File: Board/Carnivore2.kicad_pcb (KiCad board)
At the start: 2 copper layers, 157 parts, among them T1 2SC945, T2 2SA733, T3 2SC945, T4 2SC945, T5 2SC945, T6 2SA733, U7 50 MHz

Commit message: Schematic and pcb conversion cleanup and rework
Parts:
- removed ?: , 
- removed LED2, LED3, LED4: , C_0603_1
- AU1, AU2, LED1, U1, U2, U3, U4, U5, U6, XC1: value (none) -> ~
- B1: renamed from ?; value (none) -> BAT
- H1, H2: renamed from ?; value (none) -> MountingHole
- J1: renamed from .3; value (none) -> Conn_01x02_Pin
- TP1, TP2: renamed from ?; value (none) -> TestPoint
- U8: renamed from .1; value (none) -> DNI; footprint KNS01_1 -> Oscillator:Oscillator_SMD_TXC_7C-4Pin_5.0x3.2mm_HandSoldering
- X1: renamed from .2; value (none) -> EDGE50/MSX
- X2: renamed from .6; value (none) -> HEADER_5X2; footprint IDC10M_1 -> HDR2X5
- X3: renamed from .7; value (none) -> HEADER_5X2; footprint IDC10M_1 -> HDR2X5
- moved U8 3.69 mm to (144.3, 76.5), turned to 180 degrees
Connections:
- net +AV12 renamed /AV12+
- net -AV12 renamed /AV12-
- net -V12 renamed /VCC-12
- net A0 renamed Net-(R9-Pad2)
- net A1 renamed Net-(R36-Pad2)
- net A10 renamed Net-(R13-Pad2)
- net A11 renamed Net-(R32-Pad2)
- net A12 renamed Net-(R34-Pad2)
- net A13 renamed Net-(R10-Pad2)
- net A14 renamed Net-(R35-Pad2)
- net A15 renamed Net-(R14-Pad2)
- net A2 renamed Net-(R8-Pad2)
- net A3 renamed Net-(R37-Pad2)
- net A4 renamed Net-(R7-Pad2)
- net A5 renamed Net-(R38-Pad2)
- net A6 renamed Net-(R12-Pad2)
- net A7 renamed Net-(R33-Pad2)
- net A8 renamed Net-(R11-Pad2)
- net A9 renamed Net-(R31-Pad2)
- net ADSO renamed /ASDO
- net BICK renamed /BICK
- net CE2 renamed Net-(D4-K)
- net CF_LED renamed Net-(LED1-K)
- net CKS renamed /CKS
- net CLC renamed Net-(R2-Pad2)
- net CONF_DONE renamed /CONF_DONE
- net D0 renamed Net-(R6-Pad2)
- net D1 renamed Net-(R39-Pad2)
- net D2 renamed Net-(R5-Pad2)
- net D3 renamed Net-(R40-Pad2)
- net D4 renamed Net-(R4-Pad2)
- net D5 renamed Net-(R41-Pad2)
- net D6 renamed Net-(R3-Pad2)
- net D7 renamed Net-(R42-Pad2)
- net DATA0 renamed /DATA0
- net DCLK renamed /DCLK
- net EECK renamed /EECK
- net EECS renamed /EECS
- net EEDI renamed /EEDI
- net EEDO renamed /EEDO
- net HD10 renamed /HD10
- net HD11 renamed /HD11
- net HD12 renamed /HD12
- net HD13 renamed /HD13
- net HD14 renamed /HD14
- net HD15 renamed /HD15
- net HD3 renamed /HD03
- net HD4 renamed /HD04
- net HD5 renamed /HD05
- net HD6 renamed /HD06
- net HD7 renamed /HD07
- net KN0 renamed /KN0
- net LAUDIOR renamed Net-(T5-E)
- net LAUDOL renamed Net-(T3-E)
- net LRCK renamed /LRCK
- net MCLK renamed /MCLK
- net NCE renamed /NCE
- net NCONFIG renamed /NCONFIG
- net NCS0 renamed /NCSO
- net NET00000 renamed /CLC50
- net NET00004 renamed Net-(T1-B)
- net NET00005 renamed Net-(T1-C)
- net NET00006 renamed Net-(T2-B)
- net NET00007 renamed Net-(X1-Pad44)
- net NET00008 renamed Net-(T2-C)
- net NET00018 renamed Net-(U1D-VCCA_PLL1)
- net NET00019 renamed Net-(U1D-VCCA_PLL2)
- net NET00020 renamed /~{HREG}
- net NET00024 renamed Net-(D3-K)
- net NET00025 renamed Net-(C23-PLUS)
- net NET00026 renamed Net-(LED1-A)
- net NET00027 renamed Net-(AU1A-IN+)
- net NET00028 renamed Net-(AU1A-IN-)
- net NET00029 renamed Net-(C102-Pad1)
- net NET00031 renamed Net-(C103-PLUS)
- net NET00033 renamed Net-(AU2A-IN-)
- net NET00036 renamed Net-(AU1B-IN+)
- net NET00037 renamed Net-(AU1B-IN-)
- net NET00038 renamed Net-(C202-Pad1)
- net NET00040 renamed Net-(C203-PLUS)
- net NET00041 renamed Net-(AU2B-IN-)
- net NET00042 renamed Net-(C205-MINUS)
- net NET00045 renamed Net-(AU2B-OUT)
- net NET00046 renamed Net-(C105-MINUS)
- net NET00047 renamed Net-(T5-B)
- net NET00048 renamed Net-(T4-B)
- net NET00049 renamed Net-(T3-B)
- net NET00050 renamed Net-(T6-C)
- net NET00051 renamed Net-(C29-PLUS)
- net NET00054 renamed Net-(U5-AOUTR)
- net NET00055 renamed Net-(U5-AOUTL)
- net NET00057 renamed Net-(C26-PLUS)
- net NET00058 renamed Net-(AU2A-OUT)
- net NSTATUS renamed Net-(U1C-nSTATUS)
- net RA0 renamed /RA00
- net RA1 renamed /RA01
- net RA10 renamed /RA10
- net RA11 renamed /RA11
- net RA12 renamed /RA12
- net RA13 renamed /RA13
- net RA14 renamed /RA14
- net RA15 renamed /RA15
- net RA16 renamed /RA16
- net RA17 renamed /RA17
- net RA18 renamed /RA18
- net RA19 renamed /RA19
- net RA2 renamed /RA02
- net RA20 renamed /RA20
- net RA21 renamed /RA21
- net RA3 renamed /RA03
- net RA4 renamed /RA04
- net RA5 renamed /RA05
- net RA6 renamed /RA06
- net RA7 renamed /RA07
- net RA8 renamed /RA08
- net RA9 renamed /RA09
- net RDQ0 renamed /RDQ0
- net RDQ1 renamed /RDQ1
- net RDQ15A-1 renamed /RDQ15A-1
- net RDQ2 renamed /RDQ2
- net RDQ3 renamed /RDQ3
- net RDQ4 renamed /RDQ4
- net RDQ5 renamed /RDQ5
- net RDQ6 renamed /RDQ6
- net RDQ7 renamed /RDQ7
- net RSW1 renamed Net-(R15-Pad2)
- net RSW2 renamed Net-(R25-Pad2)
- net RVPPE renamed /RVPPE
- net R~E renamed /R~{E}
- net R~G renamed /R~{G}
- net R~RB renamed /~{RRB}
- net R~RP renamed /~{RRP}
- net R~W renamed /~{RWR}
- net SDATA renamed /SDATA
- net SLTA0 renamed /SLT_A00
- net SLTA1 renamed /SLT_A01
- net SLTA10 renamed /SLT_A10
- net SLTA11 renamed /SLT_A11
- net SLTA12 renamed /SLT_A12
- net SLTA13 renamed /SLT_A13
- net SLTA14 renamed /SLT_A14
- net SLTA15 renamed /SLT_A15
- net SLTA2 renamed /SLT_A02
- net SLTA3 renamed /SLT_A03
- net SLTA4 renamed /SLT_A04
- net SLTA5 renamed /SLT_A05
- net SLTA6 renamed /SLT_A06
- net SLTA7 renamed /SLT_A07
- net SLTA8 renamed /SLT_A08
- net SLTA9 renamed /SLT_A09
- net SLTCLC renamed /SLT_CLC
- net SLTD0 renamed /SLT_D0
- net SLTD1 renamed /SLT_D1
- net SLTD2 renamed /SLT_D2
- net SLTD3 renamed /SLT_D3
- net SLTD4 renamed /SLT_D4
- net SLTD5 renamed /SLT_D5
- net SLTD6 renamed /SLT_D6
- net SLTD7 renamed /SLT_D7
- net SLTRSW2 renamed /RSW2
- net SLTSOUND renamed /SLTSOUND
- net SLT_MREQ renamed /~{SLT_MREQ}
- net SLT~BUSDIR renamed /~{SLT_BUSDIR}
- net SLT~CS1 renamed /~{SLT_CS1}
- net SLT~CS12 renamed /~{SLT_CS12}
- net SLT~CS2 renamed /~{SLT_CS2}
- net SLT~INT renamed /~{SLT_INT}
- net SLT~IORQ renamed /~{SLT_IORQ}
- net SLT~M1 renamed /~{SLT_M1}
- net SLT~RD renamed /~{SLT_RD}
- net SLT~RFSH renamed /~{SLT_RFSH}
- net SLT~SLTSL renamed /~{SLT_SLTSEL}
- net SLT~WAIT renamed /~{SLT_WAIT}
- net SLT~WR renamed /~{SLT_WR}
- net STLRSW1 renamed /RSW1
- net TCK renamed /TCK
- net TDI renamed /TDI
- net TDO renamed /TDO
- net TMS renamed /TMS
- net V1.2 renamed /VCC1.2
- net V12 renamed /VCC+12
- net VCCRAM renamed Net-(D1-K)
- net VDDDA renamed /VCC3.3A
- net VPP12 renamed Net-(U2-Vpp/~{WP})
- net ~BUSDIR renamed Net-(R18-Pad2)
- net ~CS1 renamed Net-(R23-Pad2)
- net ~CS12 renamed Net-(R24-Pad2)
- net ~CS2 renamed Net-(R22-Pad2)
- net ~CSRAM renamed /~{CSRAM}
- net ~HCS1 renamed /~{HCS1}
- net ~HCS3 renamed /~{HCS3}
- net ~HRD renamed /~{HRD}
- net ~HRST renamed /~{HRST}
- net ~IC renamed /~{IC}
- net ~INT renamed Net-(R19-Pad2)
- net ~IORQ renamed Net-(R28-Pad2)
- net ~M1 renamed Net-(R27-Pad2)
- net ~MREQ renamed Net-(R17-Pad2)
- net ~RD renamed Net-(R16-Pad2)
- net ~RFSH renamed Net-(R20-Pad2)
- net ~SLTSL renamed Net-(R21-Pad2)
- net ~WAIT renamed Net-(R26-Pad2)
- net ~WR renamed Net-(R29-Pad2)
- AU2 pad 3: GND -> /GND
- AU2 pad 5: GND -> /GND
- AX1 pad 1: GND -> /GND
- C1 pad 1: GND -> /GND
- C1 pad 2: VCC5 -> /VCC5
- C10 pad 1: V3.3 -> /VCC3.3
- C10 pad 2: GND -> /GND
- C101 pad 1: GND -> /GND
- C102 pad 2: GND -> /GND
- C11 pad 2: GND -> /GND
- C12 pad 1: GND -> /GND
- C13 pad 1: GND -> /GND
- C14 pad 2: GND -> /GND
- C15 pad 2: GND -> /GND
- C16 pad 1: GND -> /GND
- C16 pad 2: V3.3 -> /VCC3.3
- C17 pad 2: GND -> /GND
- C18 pad 1: GND -> /GND
- C19 pad 2: GND -> /GND
- C2 pad 1: GND -> /GND
- C2 pad 2: V3.3 -> /VCC3.3
- C20 pad 1: GND -> /GND
- C201 pad 1: GND -> /GND
- C202 pad 2: GND -> /GND
- C21 pad 2: GND -> /GND
- C22 pad 1: GND -> /GND
- C23 pad 1: GND -> /GND
- C24 pad 1: GND -> /GND
- C25 pad 1: GND -> /GND
- C26 pad 1: GND -> /GND
- C27 pad 1: GND -> /GND
- C28 pad 1: GND -> /GND
- C28 pad 2: NET00053 -> Net-(C28-PLUS)
- C29 pad 1: GND -> /GND
- C3 pad 1: GND -> /GND
- C30 pad 1: GND -> /GND
- C30 pad 2: V3.3 -> /VCC3.3
- C4 pad 1: GND -> /GND
- C4 pad 2: V3.3 -> /VCC
- C5 pad 1: GND -> /GND
- C5 pad 2: V3.3 -> /VCC
- C6 pad 1: GND -> /GND
- C7 pad 1: GND -> /GND
- C7 pad 2: V3.3 -> /VCC3.3
- C8 pad 1: GND -> /GND
- C8 pad 2: V3.3 -> /VCC3.3
- C9 pad 1: GND -> /GND
- C9 pad 2: V3.3 -> /VCC3.3
- D1 pad 1: V3.3 -> /VCC3.3
- D2 pad 1: NET00022 -> Net-(D2-A)
- D3 pad 1: V3.3 -> /VCC3.3
- D5 pad 1: NET00053 -> Net-(D5-A)
- D5 pad 2: ~RESET -> /~{SLT_RESET}
- D6 pad 1: VCC5 -> /VCC5
- R30 pad 1: SLT~RESET -> /~{SLT_RESET}
- R30 pad 2: ~RESET -> Net-(R30-Pad2)
- R45 pad 2: V3.3 -> /VCC3.3
- R46 pad 1: GND -> /GND
- R47 pad 1: V3.3 -> /VCC3.3
- R48 pad 1: V3.3 -> /VCC3.3
- R50 pad 1: GND -> /GND
- R51 pad 1: NET00023 -> Net-(B1-PadPOS)
- R51 pad 2: NET00022 -> Net-(D2-A)
- R57 pad 1: GND -> /GND
- R58 pad 1: V3.3 -> /VCC3.3
- R59 pad 1: V3.3 -> /VCC3.3
- R60 pad 1: NET00052 -> Net-(C28-PLUS)
- R60 pad 2: NET00053 -> Net-(D5-A)
- R65 pad 1: VCC5 -> /VCC5
- R65 pad 2: NET00052 -> Net-(C28-PLUS)
- R66 pad 2: V3.3 -> /VCC3.3
- T1 pad A2: GND -> /GND
- T3 pad K: GND -> /GND
- T4 pad K: GND -> /GND
- T5 pad K: GND -> /GND
- T6 pad A1: NET00052 -> Net-(C28-PLUS)
- U1 pad 10: (no net) -> unconnected-(U1A-IO,_LVDS7n,_DQ1L1/_-Pad10)
- U1 pad 100: GND -> /GND
- U1 pad 107: (no net) -> unconnected-(U1B-IO,_LVDS41n_(INIT_DONE)-Pad107)
- U1 pad 109: V3.3 -> /VCC3.3
- U1 pad 11: (no net) -> unconnected-(U1A-IO,_LVDS6p,_DQ1L2/_-Pad11)
- U1 pad 111: GND -> /GND
- U1 pad 122: V3.3 -> /VCC3.3
- U1 pad 124: GND -> /GND
- U1 pad 125: GND -> /GND
- U1 pad 126: GND -> /GND
- U1 pad 129: (no net) -> /GND
- U1 pad 131: (no net) -> /GND
- U1 pad 132: (no net) -> /GND
- U1 pad 136: V3.3 -> /VCC3.3
- U1 pad 140: GND -> /GND
- U1 pad 148: V3.3 -> /VCC3.3
- U1 pad 153: GND -> /GND
- U1 pad 154: GND -> /GND
- U1 pad 156: GND -> /GND
- U1 pad 158: GND -> /GND
- U1 pad 159: GND -> /GND
- U1 pad 166: V3.3 -> /VCC3.3
- U1 pad 167: GND -> /GND
- U1 pad 170: HD9 -> /HD09
- U1 pad 171: HD2 -> /HD02
- U1 pad 172: V3.3 -> /VCC3.3
- U1 pad 173: HD8 -> /HD08
- U1 pad 174: GND -> /GND
- U1 pad 175: HD1 -> /HD01
- U1 pad 176: HD0 -> /HD00
- U1 pad 177: GND -> /GND
- U1 pad 179: HA0 -> /~{HA0}
- U1 pad 181: HA1 -> /~{HA1}
- U1 pad 182: HA2 -> /~{HA2}
- U1 pad 183: V3.3 -> /VCC3.3
- U1 pad 184: GND -> /GND
- U1 pad 186: GND -> /GND
- U1 pad 188: ~HWR -> /~{HVR}
- U1 pad 189: (no net) -> unconnected-(U1A-IO,_LVDS19n,_DQ1T2/DQ1T11-Pad189)
- U1 pad 194: V3.3 -> /VCC3.3
- U1 pad 196: GND -> /GND
- U1 pad 202: V3.3 -> /VCC3.3
- U1 pad 204: GND -> /GND
- U1 pad 23: (no net) -> /GND
- U1 pad 24: (no net) -> /GND
- U1 pad 25: GND -> /GND
- U1 pad 28: (no net) -> /GND
- U1 pad 29: V3.3 -> /VCC3.3
- U1 pad 3: (no net) -> unconnected-(U1A-IO,_LVDS9p_(CRC_ERROR)-Pad3)
- U1 pad 36: (no net) -> unconnected-(U1A-IO,_LVDS2n-Pad36)
- U1 pad 37: (no net) -> unconnected-(U1A-IO,_VREFB1N1-Pad37)
- U1 pad 38: GND -> /GND
- U1 pad 4: (no net) -> unconnected-(U1A-IO,_LVDS9n_(CLKUSR)-Pad4)
- U1 pad 40: (no net) -> unconnected-(U1A-IO,_LVDS1p,_DQ1L8/_-Pad40)
- U1 pad 41: (no net) -> unconnected-(U1A-IO,_LVDS1n,_(DM1L/BWS#1L)/_-Pad41)
- U1 pad 42: V3.3 -> /VCC3.3
- U1 pad 43: (no net) -> unconnected-(U1A-IO-Pad43)
- U1 pad 44: (no net) -> unconnected-(U1A-IO,_LVDS0p-Pad44)
- U1 pad 46: (no net) -> unconnected-(U1A-IO-Pad46)
- U1 pad 47: (no net) -> unconnected-(U1A-IO,_PLL1_OUTp-Pad47)
- U1 pad 48: (no net) -> unconnected-(U1A-IO,_PLL1_OUTn-Pad48)
- U1 pad 49: GND -> /GND
- U1 pad 5: (no net) -> unconnected-(U1A-IO,_LVDS8p-Pad5)
- U1 pad 50: GND -> /GND
- U1 pad 52: GND -> /GND
- U1 pad 54: GND -> /GND
- U1 pad 55: GND -> /GND
- U1 pad 6: (no net) -> unconnected-(U1A-IO,_LVDS8n-Pad6)
- U1 pad 62: V3.3 -> /VCC3.3
- U1 pad 65: GND -> /GND
- U1 pad 7: V3.3 -> /VCC3.3
- U1 pad 71: V3.3 -> /VCC3.3
- U1 pad 73: GND -> /GND
- U1 pad 78: GND -> /GND
- U1 pad 8: (no net) -> unconnected-(U1A-IO,_LVDS7p,_DQ1L0/_-Pad8)
- U1 pad 83: V3.3 -> /VCC3.3
- U1 pad 85: GND -> /GND
- U1 pad 89: SLT~RESET -> /~{SLT_RESET}
- U1 pad 9: GND -> /GND
- U1 pad 91: V3.3 -> /VCC3.3
- U1 pad 93: GND -> /GND
- U1 pad 98: V3.3 -> /VCC3.3
- U2 pad 27: GND -> /GND
- U2 pad 30: RDQ8 -> unconnected-(U2-D8-Pad30)
- U2 pad 32: RDQ9 -> unconnected-(U2-D9-Pad32)
- U2 pad 34: RDQ10 -> unconnected-(U2-D10-Pad34)
- U2 pad 36: RDQ11 -> unconnected-(U2-D11-Pad36)
- U2 pad 37: V3.3 -> /VCC3.3
- U2 pad 39: RDQ12 -> unconnected-(U2-D12-Pad39)
- U2 pad 41: RDQ13 -> unconnected-(U2-D13-Pad41)
- U2 pad 43: RDQ14 -> unconnected-(U2-D14-Pad43)
- U2 pad 46: GND -> /GND
- U2 pad 47: GND -> /GND
- U3 pad 10: (no net) -> unconnected-(U3-NC-Pad10)
- U3 pad 13: (no net) -> unconnected-(U3-DNU-Pad13)
- U3 pad 14: (no net) -> unconnected-(U3-~{BNE}-Pad14)
- U3 pad 15: (no net) -> unconnected-(U3-~{BLE}-Pad15)
- U3 pad 27: GND -> /GND
- U3 pad 30: (no net) -> unconnected-(U3-D8-Pad30)
- U3 pad 32: (no net) -> unconnected-(U3-D9-Pad32)
- U3 pad 34: (no net) -> unconnected-(U3-D10-Pad34)
- U3 pad 36: (no net) -> unconnected-(U3-D11-Pad36)
- U3 pad 39: (no net) -> unconnected-(U3-D12-Pad39)
- U3 pad 41: (no net) -> unconnected-(U3-D13-Pad41)
- U3 pad 43: (no net) -> unconnected-(U3-D14-Pad43)
- U3 pad 46: GND -> /GND
- U3 pad 47: GND -> /GND
- U4 pad 3: V3.3 -> /VCC3.3
- U4 pad 4: GND -> /GND
- U4 pad 7: V3.3 -> /VCC3.3
- U4 pad 8: V3.3 -> /VCC3.3
- U5 pad 1: GND -> /GND
- U5 pad 11: (no net) -> unconnected-(U5-nc-Pad11)
- U5 pad 12: (no net) -> unconnected-(U5-nc-Pad12)
- U5 pad 13: (no net) -> unconnected-(U5-nc-Pad13)
- U5 pad 14: (no net) -> unconnected-(U5-nc-Pad14)
- U5 pad 19: GND -> /GND
- U5 pad 20: (no net) -> unconnected-(U5-nc-Pad20)
- U5 pad 21: (no net) -> unconnected-(U5-nc-Pad21)
- U5 pad 23: GND -> /GND
- U5 pad 24: (no net) -> unconnected-(U5-TST2-Pad24)
- U5 pad 3: GND -> /GND
- U6 pad 5: GND -> /GND
- U6 pad 6: GND -> /GND
- U6 pad 7: (no net) -> unconnected-(U6-DU-Pad7)
- U6 pad 8: V3.3 -> /VCC3.3
- U7 pad 1: (no net) -> unconnected-(U7-~{ST}-Pad1)
- U7 pad 2: GND -> /GND
- U7 pad 4: V3.3 -> /VCC3.3
- U8 pad 1: (no net) -> unconnected-(U8-~{ST}-Pad1)
- U8 pad 2: (no net) -> /GND
- U8 pad 4: GND -> /VCC3.3
- UCT1 pad 1: GND -> /GND
- UCT1 pad 3: VCC5 -> /VCC5
- UCT2 pad 1: GND -> /GND
- UCT2 pad 2: V3.3 -> /VCC3.3
- UCT2 pad 3: VCC5 -> /VCC5
- UCT2 pad 4: V3.3 -> /VCC3.3
- UCT3 pad 1: GND -> /GND
- UCT3 pad 3: VCC5 -> /VCC5
- X1 pad 15: ~RESET -> Net-(R30-Pad2)
- X1 pad 41: GND -> /GND
- X1 pad 43: GND -> /GND
- X1 pad 45: VCC5 -> /VCC5
- X1 pad 47: VCC5 -> /VCC5
- X2 pad 10: GND -> /GND
- X2 pad 2: GND -> /GND
- X2 pad 4: V3.3 -> /VCC3.3
- X3 pad 10: GND -> /GND
- X3 pad 2: GND -> /GND
- X3 pad 4: V3.3 -> /VCC3.3
- X3 pad 6: (no net) -> unconnected-(X3-Pad6)
- X3 pad 7: (no net) -> unconnected-(X3-Pad7)
- X3 pad 8: (no net) -> unconnected-(X3-Pad8)
- XC1 pad 1: GND -> /GND
- XC1 pad 10: GND -> /GND
- XC1 pad 11: GND -> /GND
- XC1 pad 12: GND -> /GND
- XC1 pad 13: V3.3 -> /VCC
- XC1 pad 14: GND -> unconnected-(XC1-Pad14)
- XC1 pad 15: GND -> /GND
- XC1 pad 16: GND -> /GND
- XC1 pad 17: GND -> /GND
- XC1 pad 18: HA2 -> /HA2
- XC1 pad 19: HA1 -> /HA1
- XC1 pad 20: HA0 -> /HA0
- XC1 pad 21: HD0 -> /HD0
- XC1 pad 22: HD1 -> /HD1
- XC1 pad 23: HD2 -> /HD2
- XC1 pad 24: (no net) -> unconnected-(XC1-Pad24)
- XC1 pad 25: (no net) -> unconnected-(XC1-Pad25)
- XC1 pad 26: (no net) -> unconnected-(XC1-Pad26)
- XC1 pad 33: GND -> /GND
- XC1 pad 35: ~HWR -> /~{HWR}
- XC1 pad 36: (no net) -> unconnected-(XC1-Pad36)
- XC1 pad 37: (no net) -> unconnected-(XC1-Pad37)
- XC1 pad 38: V3.3 -> /VCC
- XC1 pad 39: GND -> /GND
- XC1 pad 40: (no net) -> unconnected-(XC1-Pad40)
- XC1 pad 42: (no net) -> unconnected-(XC1-Pad42)
- XC1 pad 43: (no net) -> unconnected-(XC1-Pad43)
- XC1 pad 46: (no net) -> unconnected-(XC1-Pad46)
- XC1 pad 47: HD8 -> /HD8
- XC1 pad 48: HD9 -> /HD9
- XC1 pad 50: GND -> /GND
- XC1 pad 51: GND -> unconnected-(XC1-MH1-Pad51)
- XC1 pad 52: GND -> unconnected-(XC1-MH2-Pad52)
- XC1 pad 53: (no net) -> unconnected-(XC1-MH3-Pad53)
- XC1 pad 54: (no net) -> unconnected-(XC1-MH4-Pad54)
- XC1 pad 8: GND -> /GND
- XC1 pad 9: GND -> /GND
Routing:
- net (no net): track 0.00 -> 1189.4 mm, vias 2 -> 0
- net GND: track 1147.9 -> 0.00 mm, vias 41 -> 0
- net /VCC3.3: track 0.00 -> 432.6 mm, vias 0 -> 34
- net V3.3: track 426.5 -> 0.00 mm, vias 34 -> 0
- net VCC5: track 75.9 -> 0.00 mm, vias 1 -> 0
- net /VCC5: track 0.00 -> 75.9 mm, vias 0 -> 1
- net Net-(D5-A): track 0.00 -> 43.5 mm, vias 0 -> 1
- net NET00053: track 43.5 -> 0.00 mm, vias 1 -> 0
- net ~RESET: track 43.3 -> 0.00 mm
- net HA1: track 14.8 -> 0.00 mm, vias 1 -> 0
- net /HA1: track 0.00 -> 14.8 mm, vias 0 -> 1
- net HD9: track 14.8 -> 0.00 mm, vias 1 -> 0
- net /HD09: track 0.00 -> 14.8 mm, vias 0 -> 1
- net HD1: track 14.7 -> 0.00 mm, vias 1 -> 0
- net /HD1: track 0.00 -> 14.7 mm, vias 0 -> 1
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- added copper zone on B.Cu, net /GND
- added copper zone on F.Cu, net /GND
- added copper zone on F.Cu, net /VCC1.2
- added copper zone on B.Cu, net /VCC3.3
- added copper zone on F.Cu, net /VCC3.3
- added copper zone on F.Cu, net /VCC3.3A
- added copper zone on B.Cu, net unconnected-(XC1-MH3-Pad53)
- added copper zone on B.Cu, net unconnected-(XC1-MH4-Pad54)
- removed copper zone on B.Cu, net (none)
- removed copper zone on F.Cu, net (none)
- removed copper zone on F.Cu, net GND
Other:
- board outline added: 99.1 x 63.5 mm
- board text added: "Carnivore v2.2+ MSX Cartridge RBSC/TICM 2024"
- board text removed: "Carnivore v2.2 MSX Cartridge RBSC 2017"
- board text removed: "KN1"

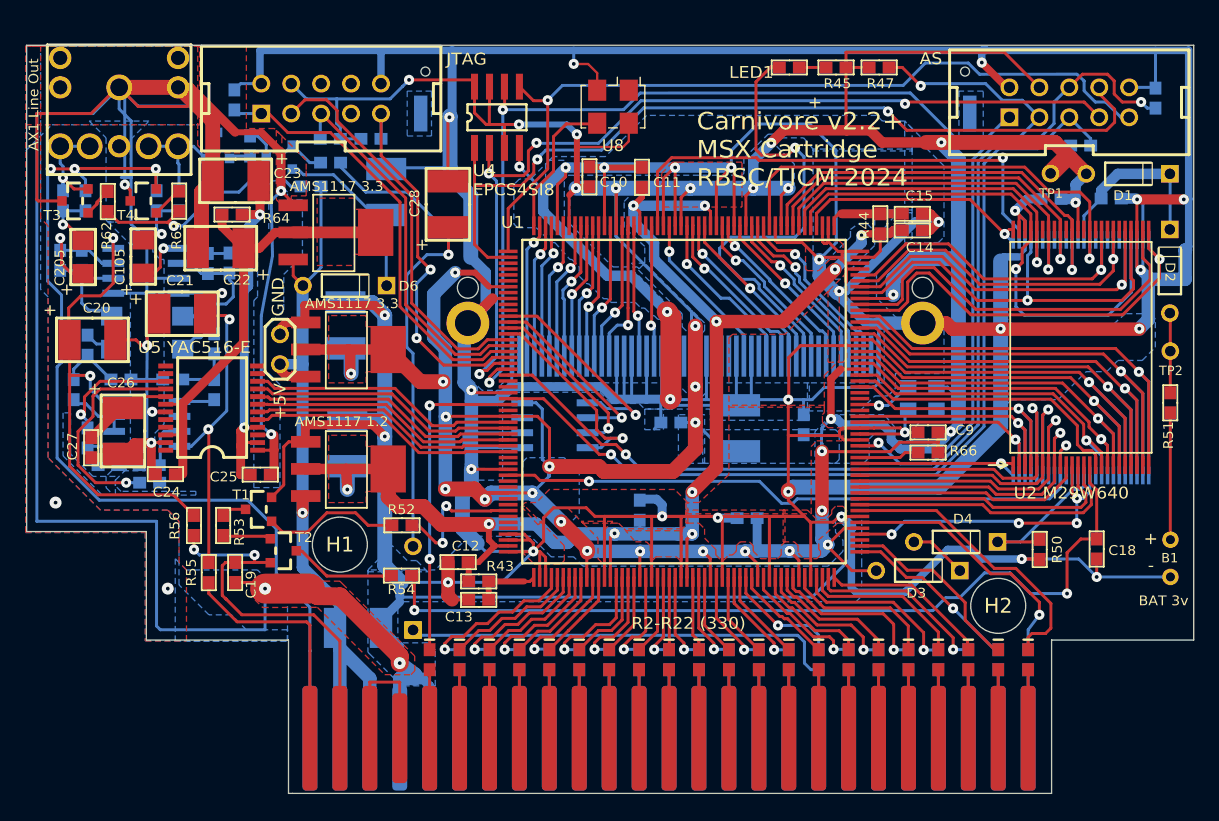
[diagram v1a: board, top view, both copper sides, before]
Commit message: Fixed lots of design rule check errors and warnings in pcb Including some serious errors: Lots of fpga GND pins unconnected, C28 connected to wrong net
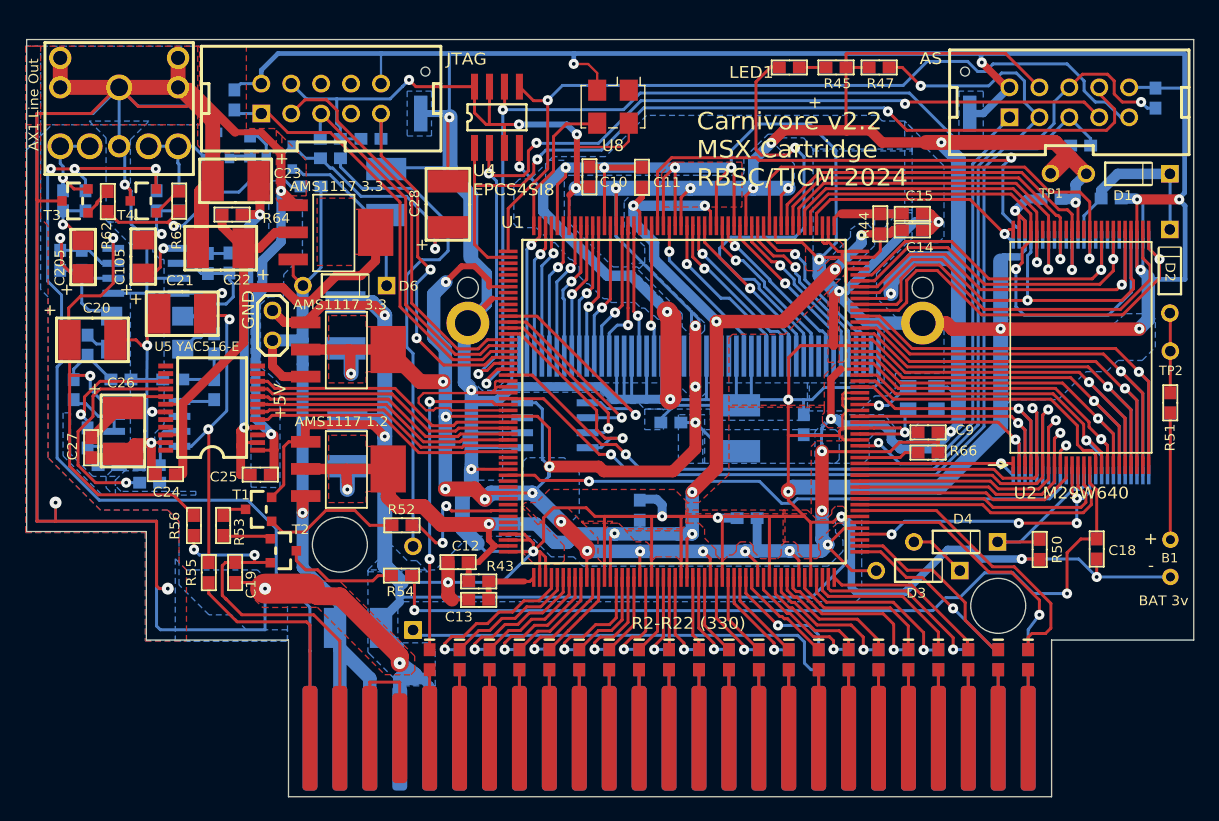
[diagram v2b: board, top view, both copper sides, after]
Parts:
- moved J1 2.11 mm to (115.4, 93.8)
- moved R60 0.37 mm to (119.5, 80.9)
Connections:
- C4 pad 2: /VCC -> /VCC3.3
- C5 pad 2: /VCC -> /VCC3.3
- D5 pad 2: /~{SLT_RESET} -> /~{SLT_RESET_RAW}
- R30 pad 2: Net-(R30-Pad2) -> /~{SLT_RESET_RAW}
- U1 pad 179: /~{HA0} -> /HA0
- U1 pad 181: /~{HA1} -> /HA1
- U1 pad 182: /~{HA2} -> /HA2
- U1 pad 188: /~{HVR} -> /~{HWR}
- X1 pad 15: Net-(R30-Pad2) -> /~{SLT_RESET_RAW}
- XC1 pad 13: /VCC -> /VCC3.3
- XC1 pad 14: unconnected-(XC1-Pad14) -> /GND
- XC1 pad 21: /HD0 -> /HD00
- XC1 pad 22: /HD1 -> /HD01
- XC1 pad 23: /HD2 -> /HD02
- XC1 pad 38: /VCC -> /VCC3.3
- XC1 pad 47: /HD8 -> /HD08
- XC1 pad 48: /HD9 -> /HD09
- XC1 pad 51: unconnected-(XC1-MH1-Pad51) -> /GND
- XC1 pad 52: unconnected-(XC1-MH2-Pad52) -> /GND
- XC1 pad 53: unconnected-(XC1-MH3-Pad53) -> /GND
- XC1 pad 54: unconnected-(XC1-MH4-Pad54) -> /GND
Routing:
- net /GND: track 3.77 -> 1229.9 mm
- net (no net): track 1189.4 -> 0.00 mm
- net /~{SLT_RESET_RAW}: track 0.00 -> 43.3 mm
- net Net-(C28-PLUS): track 8.24 -> 24.5 mm, vias 0 -> 1
- net /HD1: track 14.7 -> 0.00 mm, vias 1 -> 0
- net /HD01: track 0.00 -> 14.7 mm, vias 0 -> 1
- net /~{HWR}: track 0.00 -> 11.2 mm, vias 0 -> 1
- net /~{HVR}: track 11.2 -> 0.00 mm, vias 1 -> 0
- net /VCC3.3A: track 40.2 -> 48.8 mm
- net /VCC5: track 75.9 -> 72.5 mm
- net /VCC3.3: track 432.6 -> 430.1 mm
- net Net-(D5-A): track 43.5 -> 41.8 mm, vias 1 -> 0
- net /CONF_DONE: track 56.0 -> 57.6 mm
- net /~{CSRAM}: track 42.1 -> 43.3 mm
- net Net-(T2-C): track 8.95 -> 9.81 mm
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- removed copper zone on B.Cu, net unconnected-(XC1-MH3-Pad53)
- removed copper zone on B.Cu, net unconnected-(XC1-MH4-Pad54)
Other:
- board size 99.1 x 63.5 mm -> 99.1 x 64.3 mm
- board text added: "Carnivore v2.2 MSX Cartridge RBSC/TICM 2024"
- board text removed: "Carnivore v2.2+ MSX Cartridge RBSC/TICM 2024"

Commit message: Created local footprint library
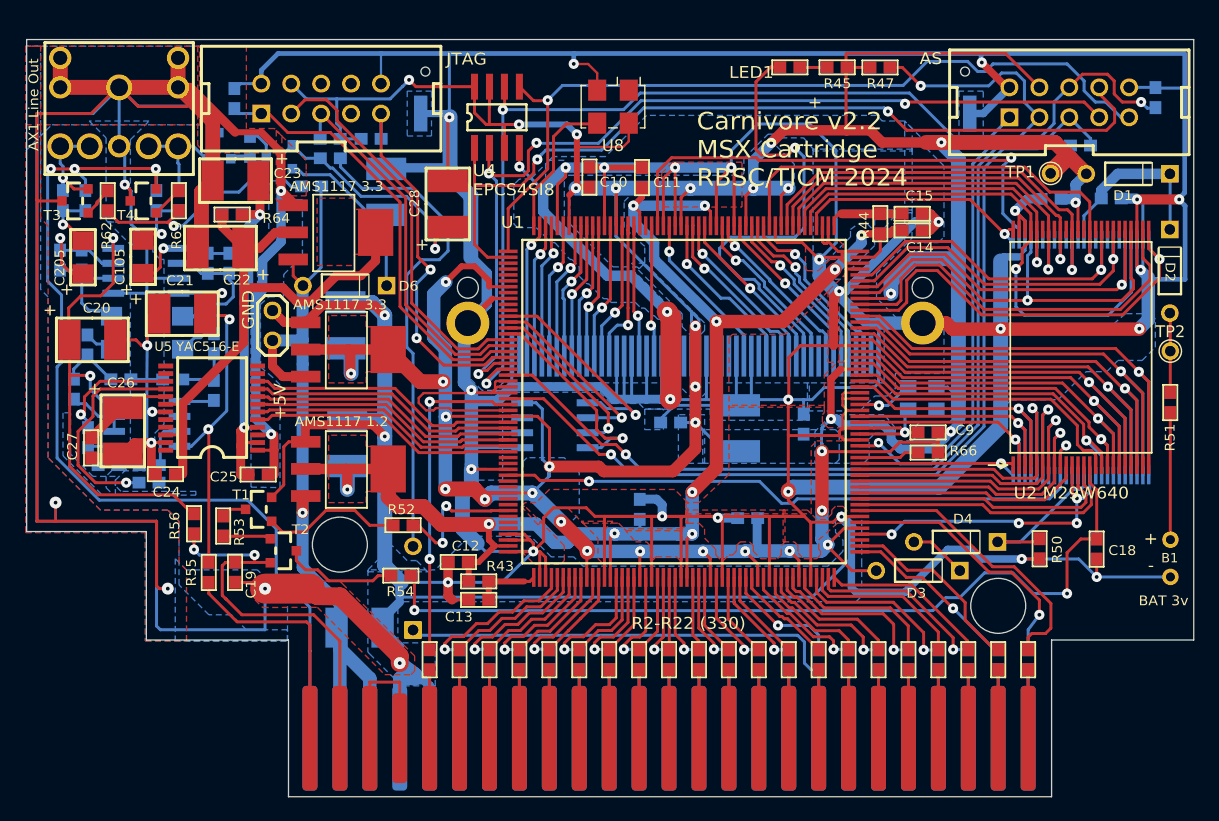
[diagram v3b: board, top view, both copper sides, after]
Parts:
- AU1, AU2: footprint 4558D_1 -> Library:4558D_1
- AX1: footprint ST-222_1 -> Library:ST-222_1
- B1: footprint (none) -> Library:BAT
- C1, C2, C20, C21, C22, C23, C26, C28, C29, C3, C4: footprint C_1812_1 -> Library:C_1812_1
- C10, C101, C102, C104, C11, C12, C13, C14, C15, C16, C17, C18, C19, C201, C202, C204, C24, C25, C27, C30, C5, C6, C7, C8, C9, LED1: footprint C_0603_1 -> Library:C_0603_1
- C103, C105, C203, C205: footprint C_1206_1 -> Library:C_1206_1
- D1, D2, D3, D4, D5, D6: footprint DIODE_1N4148_1 -> Library:DIODE_1N4148_1
- H1, H2: footprint (none) -> Library:MountingHole
- J1: footprint JUMPER_1 -> Library:JUMPER_1
- R10, R11, R12, R13, R14, R15, R16, R17, R18, R19, R2, R20, R21, R22, R23, R24, R25, R26, R27, R28, R29, R3, R30, R31, R32, R33, R34, R35, R36, R37, R38, R39, R4, R40, R41, R42, R5, R6, R7, R8, R9: footprint C0603_1 -> Library:R_0603_1
- R101, R102, R103, R104, R105, R106, R201, R202, R203, R204, R205, R206, R43, R44, R45, R46, R47, R48, R50, R51, R52, R53, R54, R55, R56, R57, R58, R59, R60, R61, R62, R63, R64, R65, R66: footprint R_0603_1 -> Library:R_0603_1
- T1, T2, T3, T4, T5, T6: footprint SOT-23(A1A2K)_1 -> Library:SOT-23(A1A2K)_1
- TP1, TP2: footprint (none) -> Library:TestPoint_THTPad_D1.5mm_Drill0.9mm
- U1: footprint EP2C5Q208C8_1 -> Library:EP2C5Q208C8_1
- U2: footprint M29W320DXXXNXX_1 -> Library:M29W320DXXXNXX_1
- U3: footprint CY62167DV30_1 -> Library:CY62167DV30_1
- U4: footprint EPCS4SI8_1 -> Library:EPCS4SI8_1
- U5: footprint YAC516-E_1 -> Library:YAC516-E_1
- U6: footprint M93C46MN1_1 -> Library:M93C46MN1_1
- U7: footprint SG-310_1 -> Library:SG-310_1
- UCT1, UCT2, UCT3: footprint ADP3338_1 -> Library:ADP3338_1
- X1: footprint EDGE50/MSX_1 -> Library:EDGE50_MSX_1
- X2, X3: footprint HDR2X5 -> Library:HDR2X5
- XC1: footprint CF-50-001_1 -> Library:CF-50-001_1
- moved C20 1.96 mm to (100.2, 96.3)
- moved C26 1.96 mm to (102.7, 104.0)
- moved C4 1.95 mm to (155.1, 103.8), turned to -90 degrees
- moved C21 1.95 mm to (107.8, 94.1)
- moved C2 1.94 mm to (121.6, 95.1), turned to -90 degrees
- moved C23 1.94 mm to (112.3, 82.8)
- moved C29 1.94 mm to (125.1, 83.8), turned to -90 degrees
- moved C3 1.93 mm to (121.8, 105.1), turned to -90 degrees
- moved C22 1.93 mm to (111.0, 88.5)
- moved C28 1.92 mm to (130.3, 84.8)
- moved C1 1.82 mm to (122.8, 120.8), turned to 180 degrees
- moved C103 1.40 mm to (107.8, 95.7)
- moved C203 1.40 mm to (101.8, 95.7)
- moved C105 1.38 mm to (104.5, 89.3), turned to -90 degrees
- moved C205 1.38 mm to (99.3, 89.3), turned to -90 degrees
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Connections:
- R10 pad 1: /SLT_A13 -> Net-(R10-Pad1)
- R10 pad 2: Net-(R10-Pad2) -> /SLT_A13
- R11 pad 1: /SLT_A08 -> Net-(R11-Pad1)
- R11 pad 2: Net-(R11-Pad2) -> /SLT_A08
- R12 pad 1: /SLT_A06 -> Net-(R12-Pad1)
- R12 pad 2: Net-(R12-Pad2) -> /SLT_A06
- R13 pad 1: /SLT_A10 -> Net-(R13-Pad1)
- R13 pad 2: Net-(R13-Pad2) -> /SLT_A10
- R14 pad 1: /SLT_A15 -> Net-(R14-Pad1)
- R14 pad 2: Net-(R14-Pad2) -> /SLT_A15
- R15 pad 1: /RSW1 -> Net-(R15-Pad1)
- R15 pad 2: Net-(R15-Pad2) -> /RSW1
- R16 pad 1: /~{SLT_RD} -> Net-(R16-Pad1)
- R16 pad 2: Net-(R16-Pad2) -> /~{SLT_RD}
- R17 pad 1: /~{SLT_MREQ} -> Net-(R17-Pad1)
- R17 pad 2: Net-(R17-Pad2) -> /~{SLT_MREQ}
- R18 pad 1: /~{SLT_BUSDIR} -> Net-(R18-Pad1)
- R18 pad 2: Net-(R18-Pad2) -> /~{SLT_BUSDIR}
- R19 pad 1: /~{SLT_INT} -> Net-(R19-Pad1)
- R19 pad 2: Net-(R19-Pad2) -> /~{SLT_INT}
- R2 pad 1: /SLT_CLC -> Net-(R2-Pad1)
- R2 pad 2: Net-(R2-Pad2) -> /SLT_CLC
- R20 pad 1: /~{SLT_RFSH} -> Net-(R20-Pad1)
- R20 pad 2: Net-(R20-Pad2) -> /~{SLT_RFSH}
- R21 pad 1: /~{SLT_SLTSEL} -> Net-(R21-Pad1)
- R21 pad 2: Net-(R21-Pad2) -> /~{SLT_SLTSEL}
- R22 pad 1: /~{SLT_CS2} -> Net-(R22-Pad1)
- R22 pad 2: Net-(R22-Pad2) -> /~{SLT_CS2}
- R3 pad 1: /SLT_D6 -> Net-(R3-Pad1)
- R3 pad 2: Net-(R3-Pad2) -> /SLT_D6
- R4 pad 1: /SLT_D4 -> Net-(R4-Pad1)
- R4 pad 2: Net-(R4-Pad2) -> /SLT_D4
- R43 pad 1: /VCC1.2 -> Net-(U1D-VCCA_PLL1)
- R43 pad 2: Net-(U1D-VCCA_PLL1) -> /VCC1.2
- R44 pad 1: Net-(U1D-VCCA_PLL2) -> /VCC1.2
- R44 pad 2: /VCC1.2 -> Net-(U1D-VCCA_PLL2)
- R45 pad 1: Net-(LED1-A) -> /VCC3.3
- R45 pad 2: /VCC3.3 -> Net-(LED1-A)
- R47 pad 1: /VCC3.3 -> /CONF_DONE
- R47 pad 2: /CONF_DONE -> /VCC3.3
- R5 pad 1: /SLT_D2 -> Net-(R5-Pad1)
- R5 pad 2: Net-(R5-Pad2) -> /SLT_D2
- R50 pad 1: /GND -> Net-(D4-K)
- R50 pad 2: Net-(D4-K) -> /GND
- R51 pad 1: Net-(B1-PadPOS) -> Net-(D2-A)
- R51 pad 2: Net-(D2-A) -> Net-(B1-PadPOS)
- R52 pad 1: Net-(T1-B) -> /RVPPE
- R52 pad 2: /RVPPE -> Net-(T1-B)
- R53 pad 1: Net-(T1-C) -> Net-(T2-B)
- R53 pad 2: Net-(T2-B) -> Net-(T1-C)
- R54 pad 1: Net-(T2-C) -> Net-(U2-Vpp/~{WP})
- R54 pad 2: Net-(U2-Vpp/~{WP}) -> Net-(T2-C)
- R55 pad 1: /AV12- -> /VCC-12
- R55 pad 2: /VCC-12 -> /AV12-
- R56 pad 1: /AV12+ -> /VCC+12
- R56 pad 2: /VCC+12 -> /AV12+
- R6 pad 1: /SLT_D0 -> Net-(R6-Pad1)
- R6 pad 2: Net-(R6-Pad2) -> /SLT_D0
- R62 pad 1: Net-(T6-C) -> Net-(T5-B)
- R62 pad 2: Net-(T5-B) -> Net-(T6-C)
- R63 pad 1: Net-(T6-C) -> Net-(T4-B)
- R63 pad 2: Net-(T4-B) -> Net-(T6-C)
- R64 pad 1: /VCC3.3A -> Net-(C23-PLUS)
- R64 pad 2: Net-(C23-PLUS) -> /VCC3.3A
- R66 pad 1: Net-(U1C-nSTATUS) -> /VCC3.3
- R66 pad 2: /VCC3.3 -> Net-(U1C-nSTATUS)
- R7 pad 1: /SLT_A04 -> Net-(R7-Pad1)
- R7 pad 2: Net-(R7-Pad2) -> /SLT_A04
- R8 pad 1: /SLT_A02 -> Net-(R8-Pad1)
- R8 pad 2: Net-(R8-Pad2) -> /SLT_A02
- R9 pad 1: /SLT_A00 -> Net-(R9-Pad1)
- R9 pad 2: Net-(R9-Pad2) -> /SLT_A00
- X1 pad 10: Net-(R18-Pad2) -> Net-(R18-Pad1)
- X1 pad 12: Net-(R17-Pad2) -> Net-(R17-Pad1)
- X1 pad 14: Net-(R16-Pad2) -> Net-(R16-Pad1)
- X1 pad 16: Net-(R15-Pad2) -> Net-(R15-Pad1)
- X1 pad 18: Net-(R14-Pad2) -> Net-(R14-Pad1)
- X1 pad 2: Net-(R22-Pad2) -> Net-(R22-Pad1)
- X1 pad 20: Net-(R13-Pad2) -> Net-(R13-Pad1)
- X1 pad 22: Net-(R12-Pad2) -> Net-(R12-Pad1)
- X1 pad 24: Net-(R11-Pad2) -> Net-(R11-Pad1)
- X1 pad 26: Net-(R10-Pad2) -> Net-(R10-Pad1)
- X1 pad 28: Net-(R9-Pad2) -> Net-(R9-Pad1)
- X1 pad 30: Net-(R8-Pad2) -> Net-(R8-Pad1)
- X1 pad 32: Net-(R7-Pad2) -> Net-(R7-Pad1)
- X1 pad 34: Net-(R6-Pad2) -> Net-(R6-Pad1)
- X1 pad 36: Net-(R5-Pad2) -> Net-(R5-Pad1)
- X1 pad 38: Net-(R4-Pad2) -> Net-(R4-Pad1)
- X1 pad 4: Net-(R21-Pad2) -> Net-(R21-Pad1)
- X1 pad 40: Net-(R3-Pad2) -> Net-(R3-Pad1)
- X1 pad 42: Net-(R2-Pad2) -> Net-(R2-Pad1)
- X1 pad 6: Net-(R20-Pad2) -> Net-(R20-Pad1)
- X1 pad 8: Net-(R19-Pad2) -> Net-(R19-Pad1)
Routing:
- net Net-(R8-Pad2): track 6.13 -> 0.00 mm
- net Net-(R8-Pad1): track 0.00 -> 6.13 mm
- net Net-(R7-Pad2): track 6.13 -> 0.00 mm
- net Net-(R7-Pad1): track 0.00 -> 6.13 mm
- net Net-(R22-Pad2): track 6.13 -> 0.00 mm
- net Net-(R22-Pad1): track 0.00 -> 6.13 mm
- net Net-(R18-Pad2): track 6.13 -> 0.00 mm
- net Net-(R18-Pad1): track 0.00 -> 6.13 mm
- net Net-(R17-Pad2): track 6.13 -> 0.00 mm
- net Net-(R17-Pad1): track 0.00 -> 6.13 mm
- net Net-(R16-Pad2): track 6.13 -> 0.00 mm
- net Net-(R16-Pad1): track 0.00 -> 6.13 mm
- net Net-(R15-Pad2): track 6.13 -> 0.00 mm
- net Net-(R15-Pad1): track 0.00 -> 6.13 mm
- net Net-(R12-Pad2): track 6.13 -> 0.00 mm
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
